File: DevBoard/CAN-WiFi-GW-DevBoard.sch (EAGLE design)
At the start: 30 parts, among them SW1 CONFIGURATION, U1 74LVC1T45GW,125, U2 74LVC1T45GW,125, U3 74LVC1T45GW,125, X1 MKDSN1,5/2-5,08

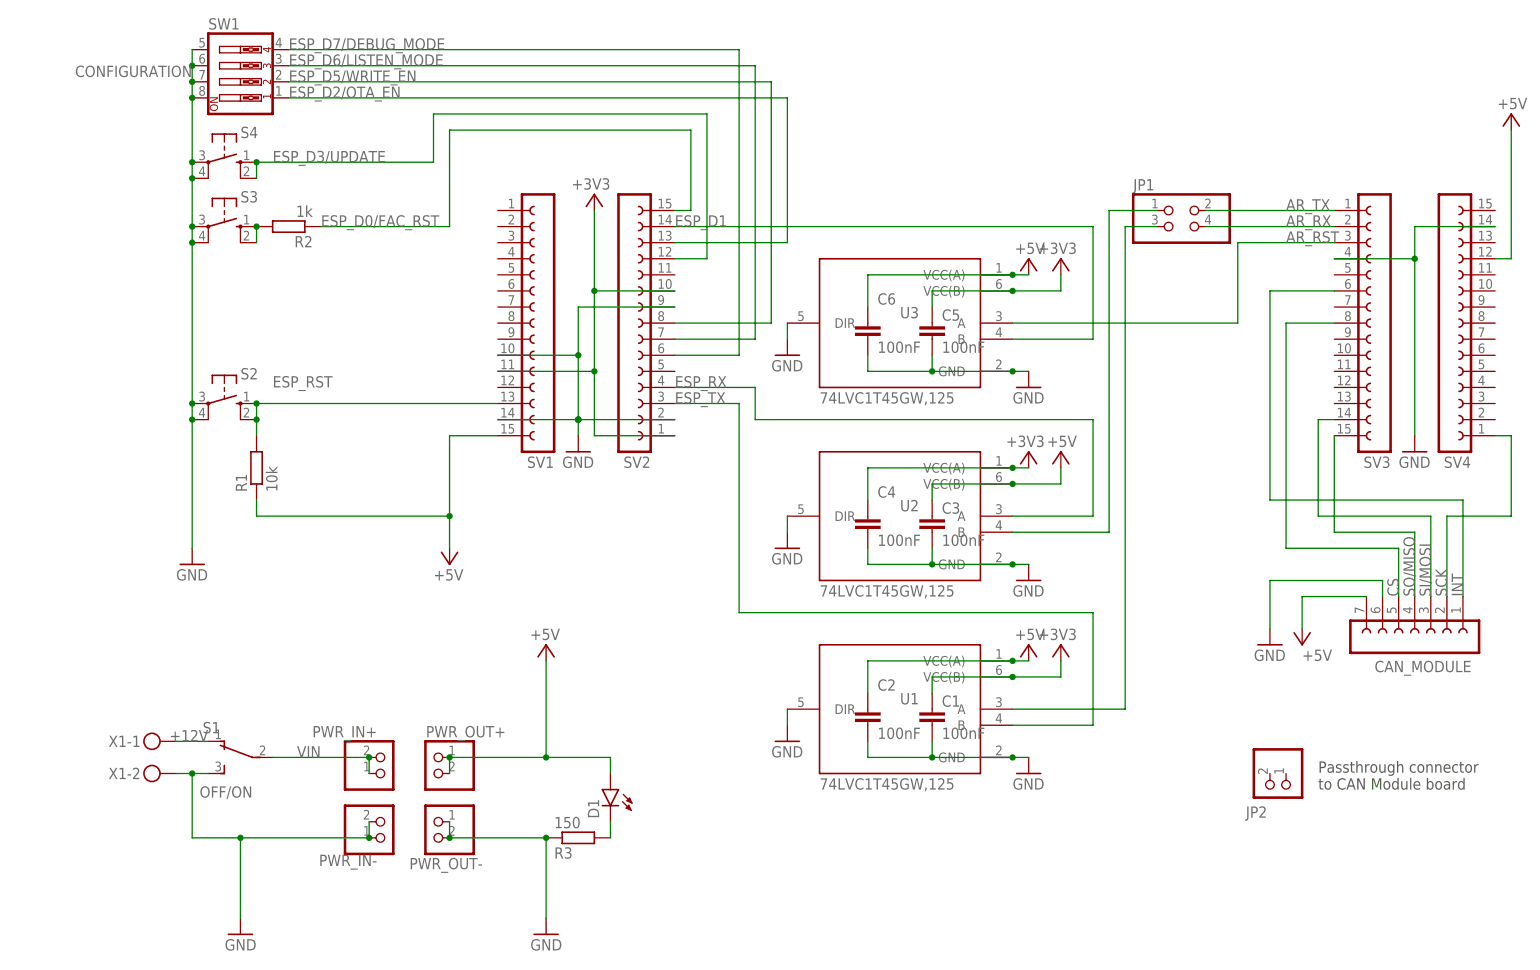
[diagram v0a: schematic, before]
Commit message: Revision dev-board fixing button mistakes, physical dimensions and robustness.
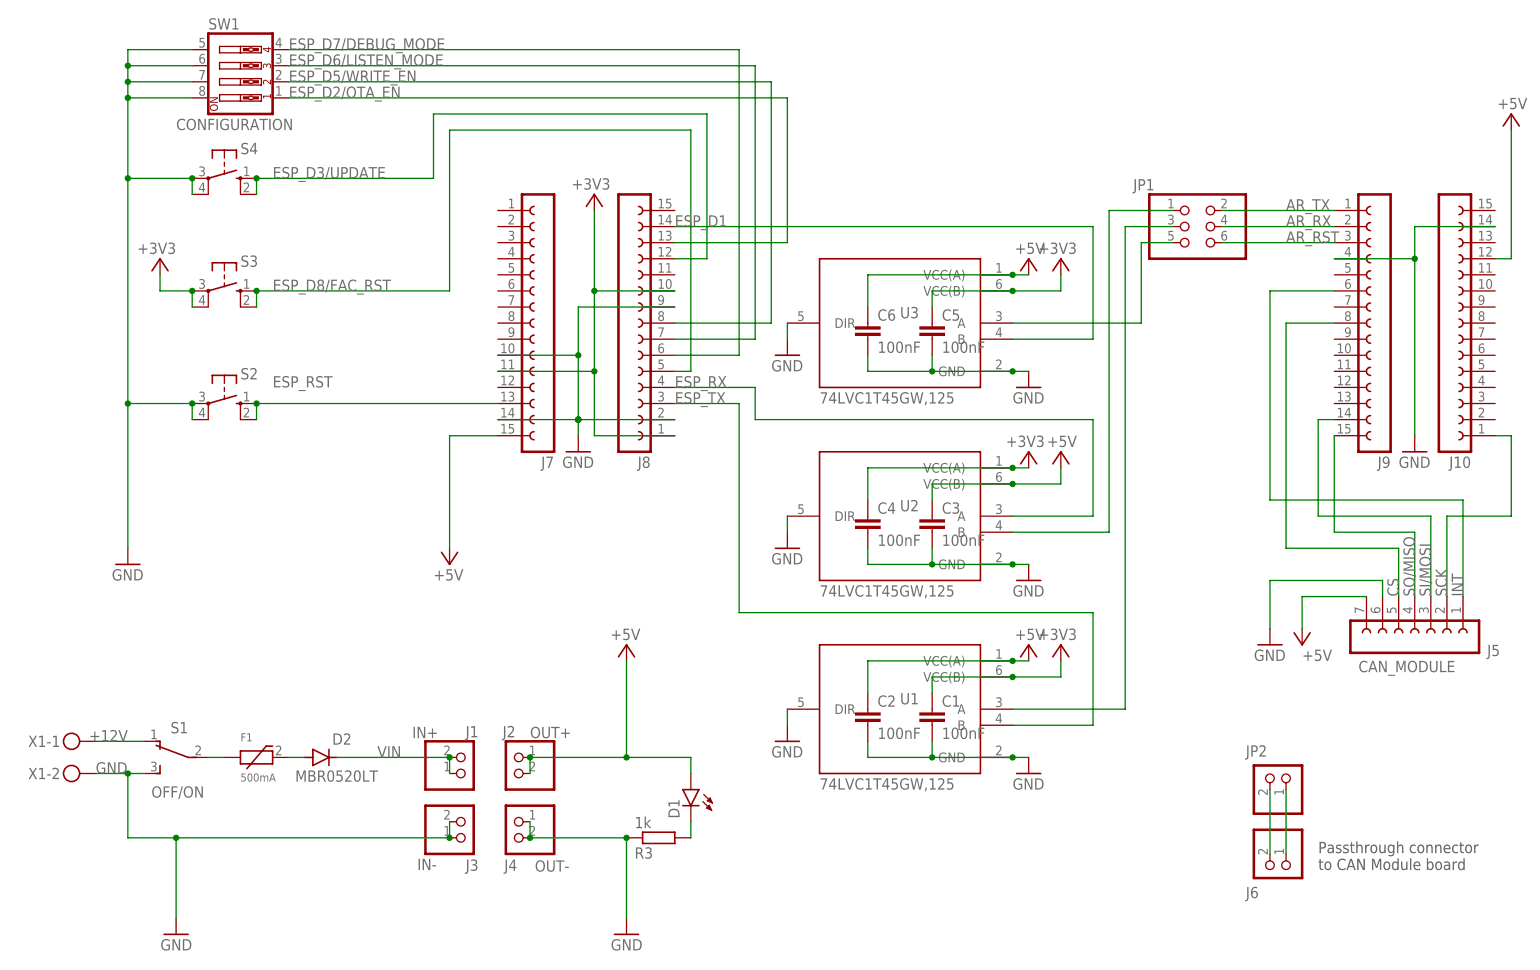
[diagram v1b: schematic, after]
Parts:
- removed PWR_IN+, PWR_IN-, PWR_OUT+, PWR_OUT-: (no value), pinhead:PINHD-1X2
- removed R1: 10k, rcl:R-EU_R1206
- removed R2: 1k, rcl:R-EU_R1206
- added D2: MBR0520LT, diode:MBR0520LT
- added F1: 500mA, custom:PTC-FUSE
- added J1: IN+, pinhead:PINHD-1X2
- added J2: OUT+, pinhead:PINHD-1X2
- added J3: IN-, pinhead:PINHD-1X2
- added J4: OUT-, pinhead:PINHD-1X2
- added J6: (no value), pinhead:PINHD-1X2
- J5: value (none) -> CAN_MODULE
- JP1: device pinhead:PINHD-2X2 -> pinhead:PINHD-2X3
- R3: value 150 -> 1k
- renumbered CAN_MODULE to J5, SV1 to J7, SV2 to J8, SV3 to J9, SV4 to J10
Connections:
- removed net ESP_D0/FAC_RST: J8.15, R2.1
- removed net FAC_RST: R2.2, S3.S, S3.S1
- new net ESP_D8/FAC_RST: J8.5, S3.S, S3.S1
- new net N$2: J6.1, JP2.1
- new net N$3: J6.2, JP2.2
- new net N$4: F1.1, S1.P
- new net N$5: D2.A, F1.2
- new net N$6: JP1.5, U3.A
- net +3V3: now also S3.P, S3.P1
- net +5V: now also J2.1, J2.2; no longer PWR_OUT+.1, PWR_OUT+.2, R1.1
- net AR_RST: now also JP1.6; no longer U3.A
- net ESP_RST: no longer R1.2
- net GND: now also J3.1, J3.2, J4.1, J4.2; no longer PWR_IN-.1, PWR_IN-.2, PWR_OUT-.1, PWR_OUT-.2, S3.P, S3.P1
- net VIN: now also D2.C, J1.1, J1.2; no longer PWR_IN+.1, PWR_IN+.2, S1.P
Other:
- moved on the sheet: D1, JP2, R3, S1, S3, S4, X1-1, X1-2

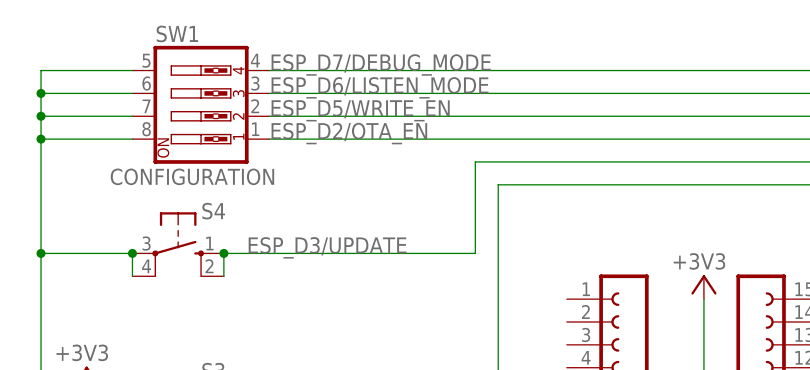
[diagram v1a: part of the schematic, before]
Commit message: Fix labelling of config switches
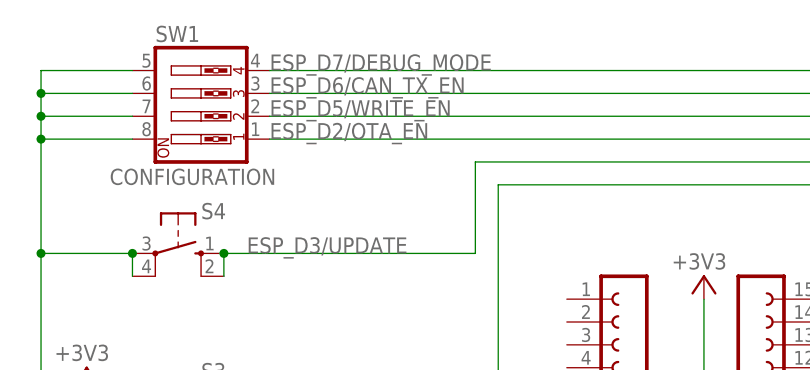
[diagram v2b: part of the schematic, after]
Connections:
- net ESP_D6/LISTEN_MODE renamed ESP_D6/CAN_TX_EN
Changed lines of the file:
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@@
 </segment>
 </net>
-<net name="ESP_D6/LISTEN_MODE" class="0">
+<net name="ESP_D6/CAN_TX_EN" class="0">
 <segment>
 <label x="27.94" y="149.86" size="1.778" layer="95"/>

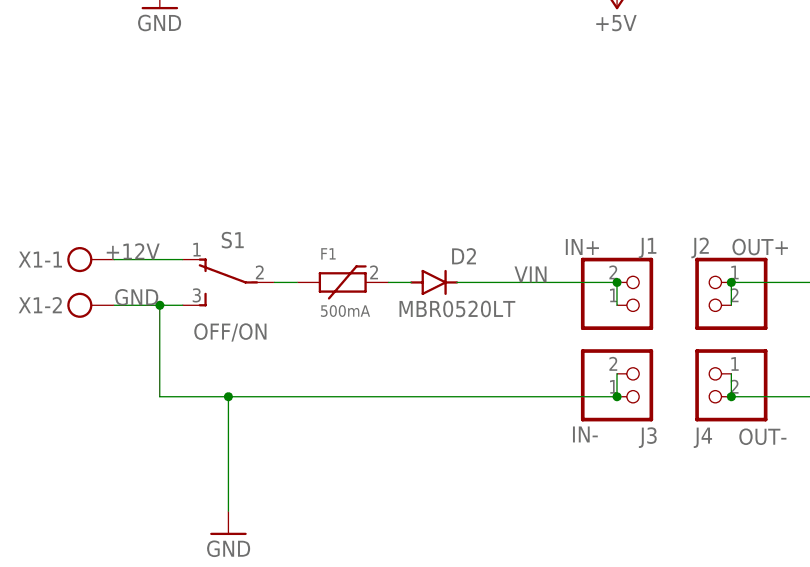
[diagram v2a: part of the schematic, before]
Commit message: Remove redundant diode before power supply
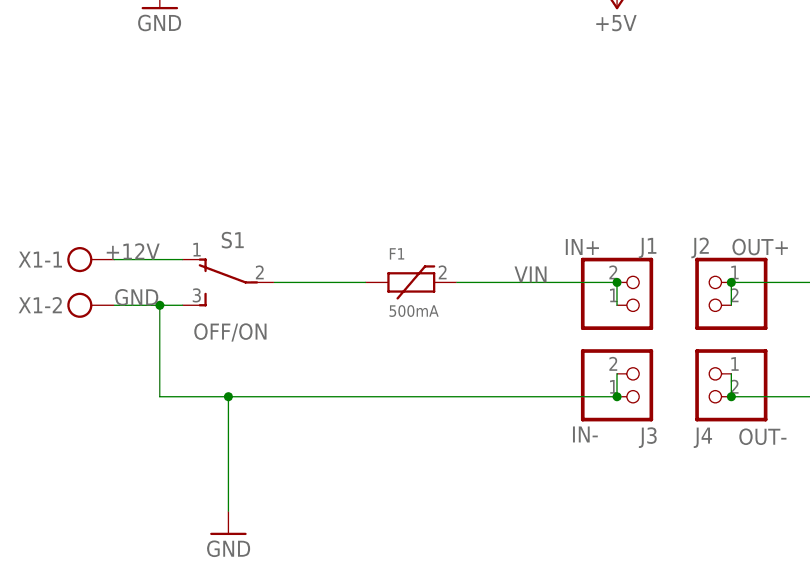
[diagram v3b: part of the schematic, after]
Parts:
- removed D2: MBR0520LT, diode:MBR0520LT
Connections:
- removed net N$5: D2.A, F1.2
- net VIN: now also F1.2; no longer D2.C
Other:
- moved on the sheet: F1
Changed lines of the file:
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@@
 <part name="+3V5" library="supply1" library_urn="urn:adsk.eagle:library:371" deviceset="+3V3" device=""/>
 <part name="F1" library="custom" deviceset="PTC-FUSE" device="" value="500mA"/>
-<part name="D2" library="diode" library_urn="urn:adsk.eagle:library:210" deviceset="MBR0520LT" device="" package3d_urn="urn:adsk.eagle:package:43420/1"/>
 </parts>
 <sheets>
@@
 <attribute name="VALUE" x="10.16" y="121.92" size="1.778" layer="96" rot="R180"/>
 </instance>
-<instance part="F1" gate="G$1" x="22.86" y="40.64" smashed="yes">
-<attribute name="NAME" x="20.32" y="43.18" size="1.27" layer="95"/>
-<attribute name="VALUE" x="20.32" y="36.83" size="1.27" layer="96"/>
-</instance>
-<instance part="D2" gate="G$1" x="33.02" y="40.64" smashed="yes">
-<attribute name="NAME" x="34.798" y="42.6466" size="1.778" layer="95"/>
-<attribute name="VALUE" x="28.956" y="36.8046" size="1.778" layer="96"/>
+<instance part="F1" gate="G$1" x="30.48" y="40.64" smashed="yes">
+<attribute name="NAME" x="27.94" y="43.18" size="1.27" layer="95"/>
+<attribute name="VALUE" x="27.94" y="36.83" size="1.27" layer="96"/>
 </instance>
 </instances>
@@
 <wire x1="53.34" y1="40.64" x2="35.56" y2="40.64" width="0.1524" layer="91"/>
 <label x="45.72" y="40.64" size="1.778" layer="95" rot="MR0"/>
-<pinref part="D2" gate="G$1" pin="C"/>
+<pinref part="F1" gate="G$1" pin="2"/>
 </segment>
 </net>
@@
 <pinref part="F1" gate="G$1" pin="1"/>
 <pinref part="S1" gate="BEF1" pin="P"/>
-<wire x1="15.24" y1="40.64" x2="17.78" y2="40.64" width="0.1524" layer="91"/>
-</segment>
-</net>
-<net name="N$5" class="0">
-<segment>
-<pinref part="D2" gate="G$1" pin="A"/>
-<pinref part="F1" gate="G$1" pin="2"/>
-<wire x1="27.94" y1="40.64" x2="30.48" y2="40.64" width="0.1524" layer="91"/>
-</segment>
-</net>
+<wire x1="15.24" y1="40.64" x2="25.4" y2="40.64" width="0.1524" layer="91"/>
+</segment>
+</net>
